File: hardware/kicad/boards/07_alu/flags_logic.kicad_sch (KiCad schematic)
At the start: 14 parts, among them U1 74AHC541, U16 74ACT151, U36 74HC86, U37 74LS08, U38 74LS540, U4 74HC688, U40 74LS377

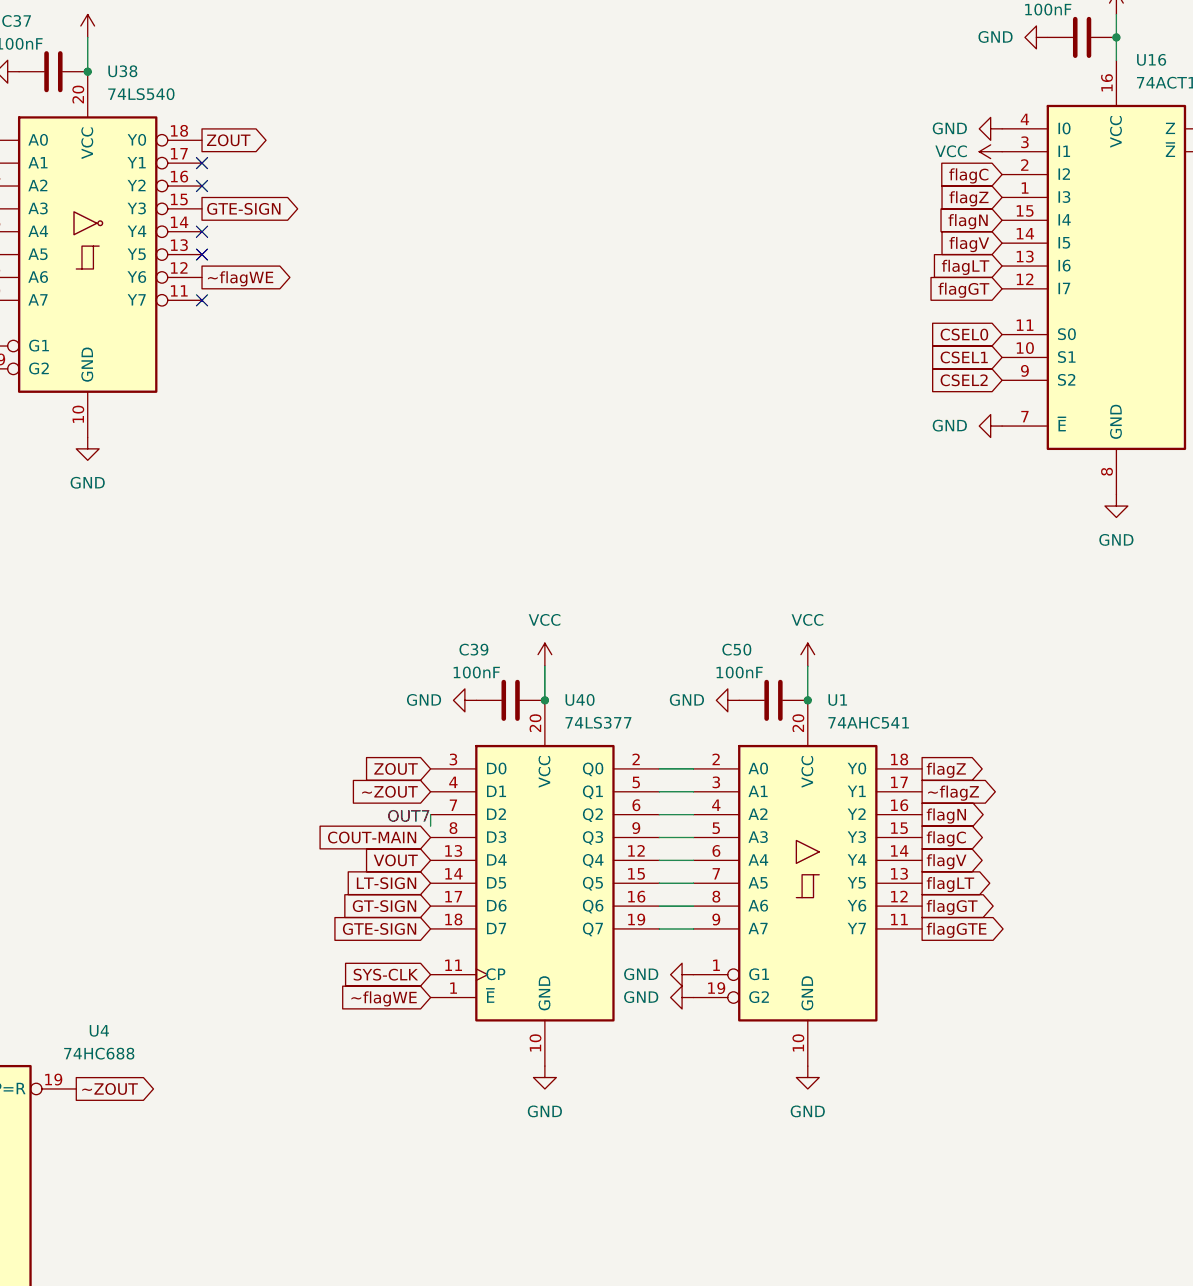
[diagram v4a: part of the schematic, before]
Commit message: checkpoint: routed all but 60 traces
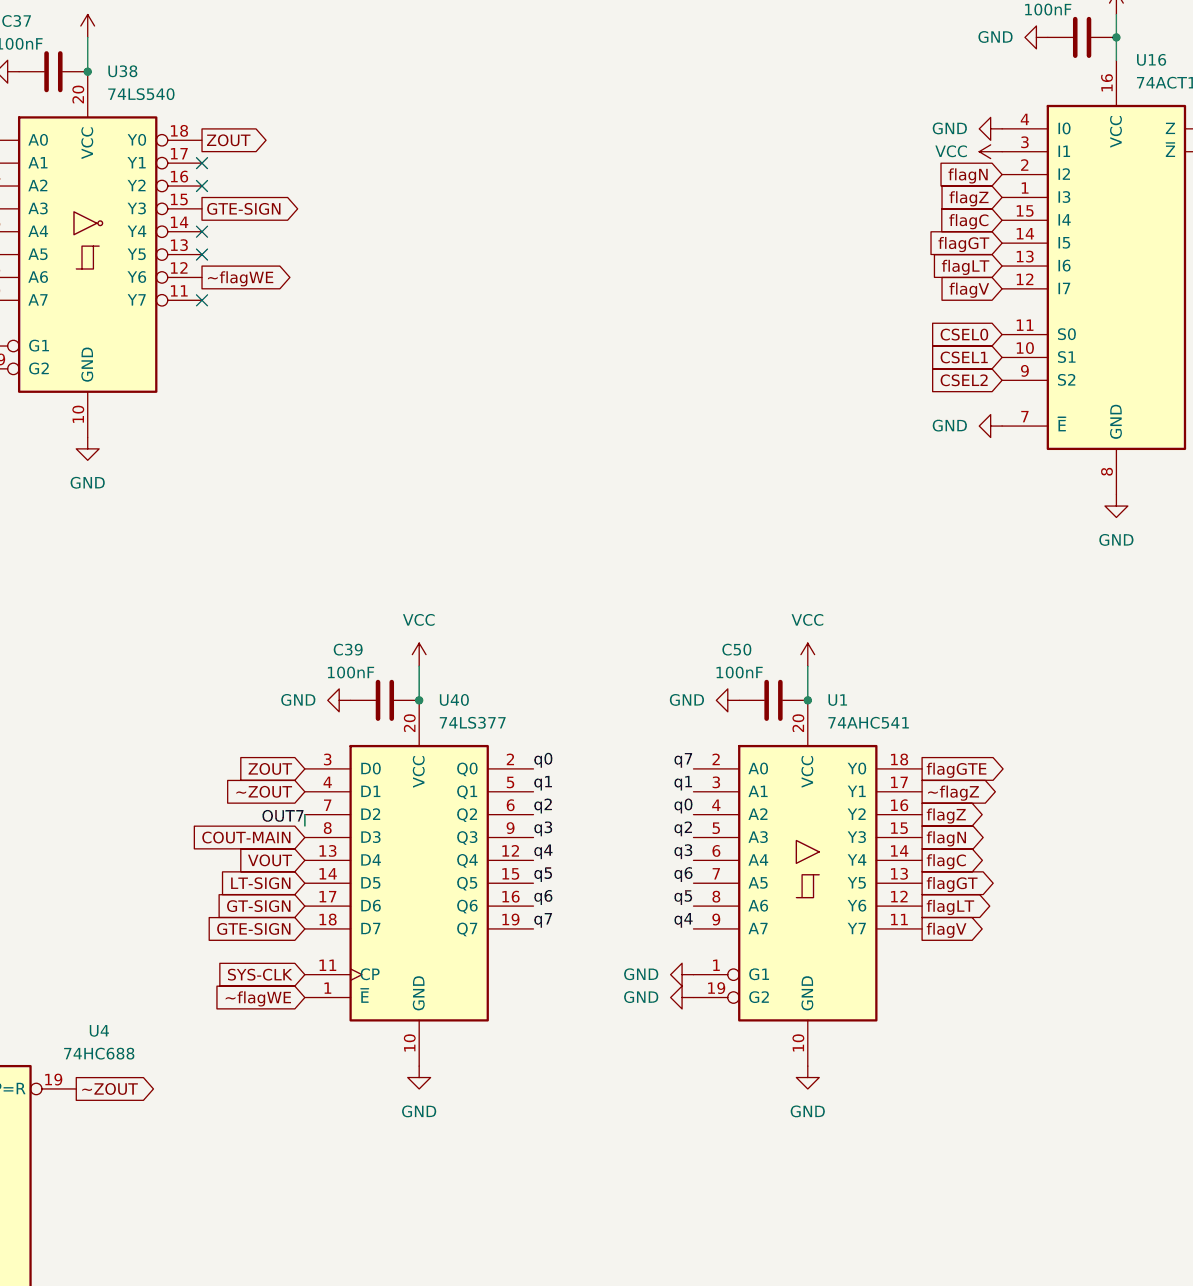
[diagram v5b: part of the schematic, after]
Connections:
- net flagC: now also U1.14 (Y4), U16.15 (I4); no longer U1.15 (Y3), U16.2 (I2)
- net flagGT: now also U1.13 (Y5), U16.14 (I5); no longer U1.12 (Y6), U16.12 (I7)
- net flagGTE: now also U1.18 (Y0); no longer U1.11 (Y7)
- net flagLT: now also U1.12 (Y6); no longer U1.13 (Y5)
- net flagN: now also U1.15 (Y3), U16.2 (I2); no longer U1.16 (Y2), U16.15 (I4)
- net flagV: now also U1.11 (Y7), U16.12 (I7); no longer U1.14 (Y4), U16.14 (I5)
- net flagZ: now also U1.16 (Y2); no longer U1.18 (Y0)
- net q3: now reaches U1.6 (A4)
- net q3: now also U40.9 (Q3); no longer U40.12 (Q4)
- net q5: now reaches U40.15 (Q5)
- net q5: now also U1.8 (A6); no longer U1.7 (A5)
- net q6: now reaches U40.16 (Q6)
- net q6: now also U1.7 (A5); no longer U1.8 (A6)
- net q4: now reaches U1.9 (A7)
- net q4: now also U40.12 (Q4); no longer U40.19 (Q7)
- net q0: now reaches U40.2 (Q0)
- net q0: now also U1.4 (A2); no longer U1.2 (A0)
- net q1: now reaches U1.3 (A1), U40.5 (Q1)
- net q2: now reaches U40.6 (Q2)
- net q2: now also U1.5 (A3); no longer U1.4 (A2)
- new net q7: U1.2 (A0), U40.19 (Q7)
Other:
- moved on the sheet: C39, U40

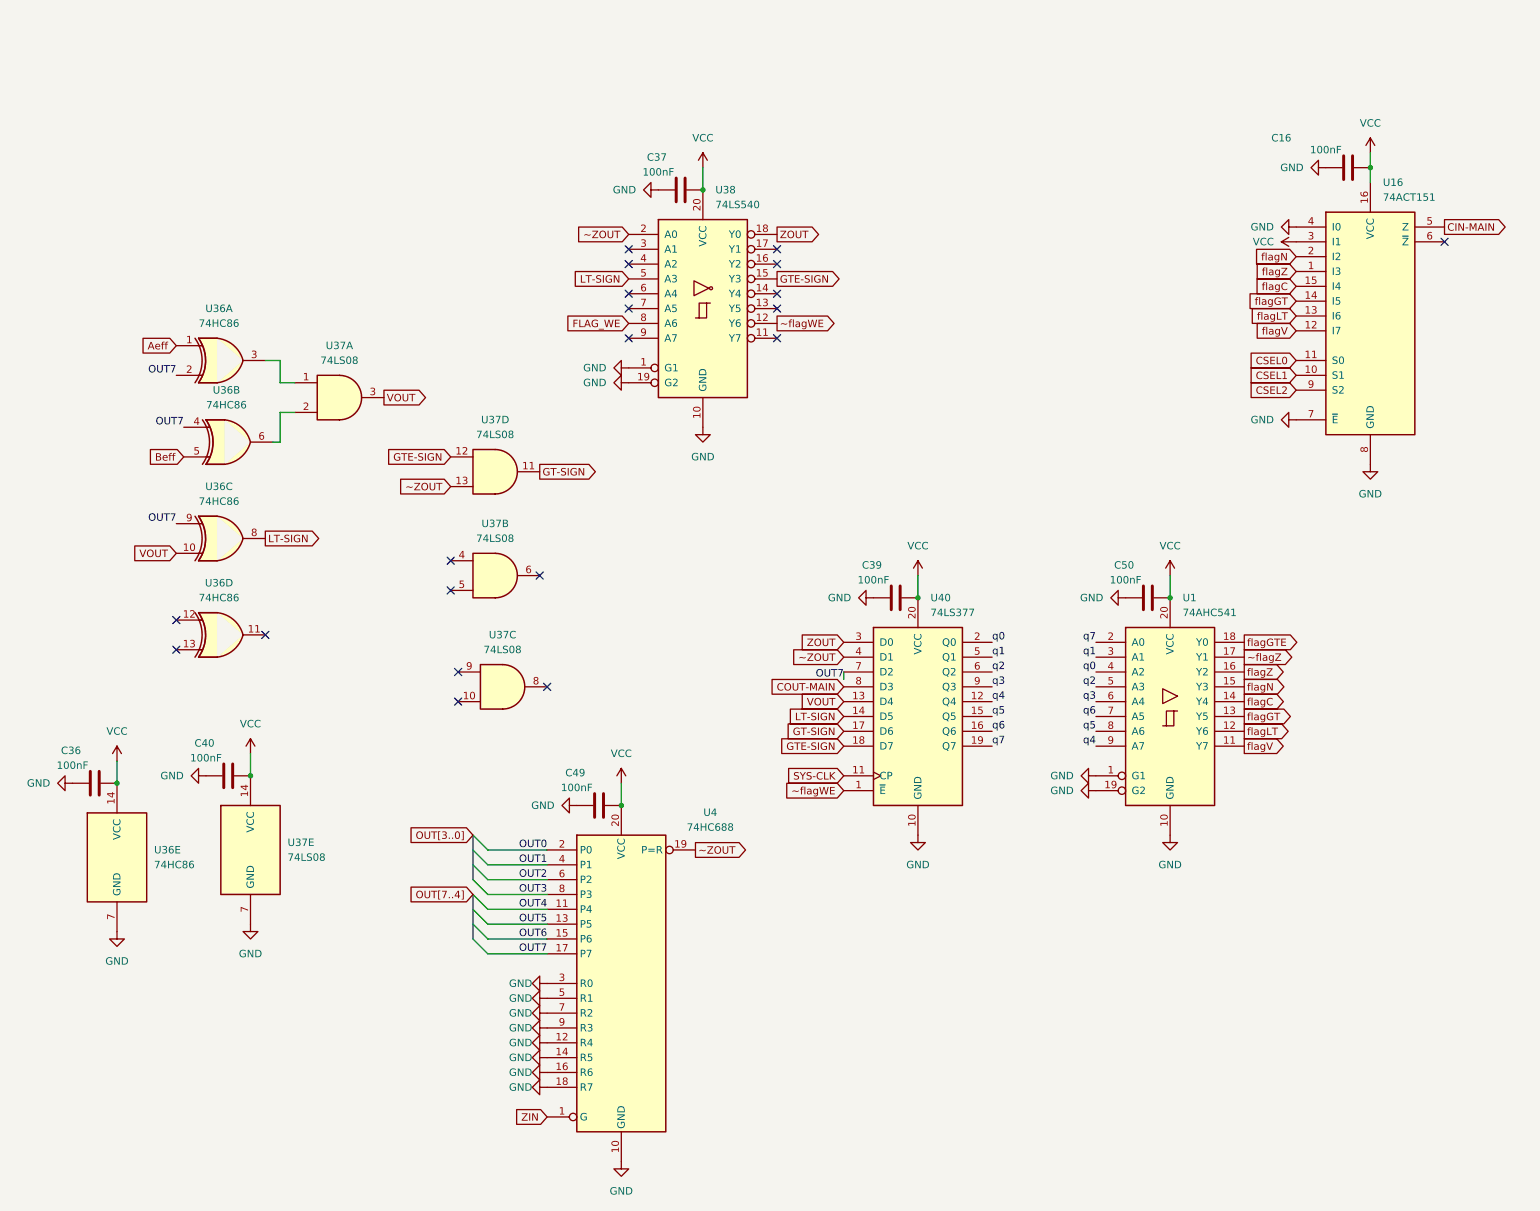
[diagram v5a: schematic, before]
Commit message: fpga: implemented fsm to brute force find matching opcode
It finds opcode by brute force sweeping across 256 by 256 and checking if computed output is equal to expected test output
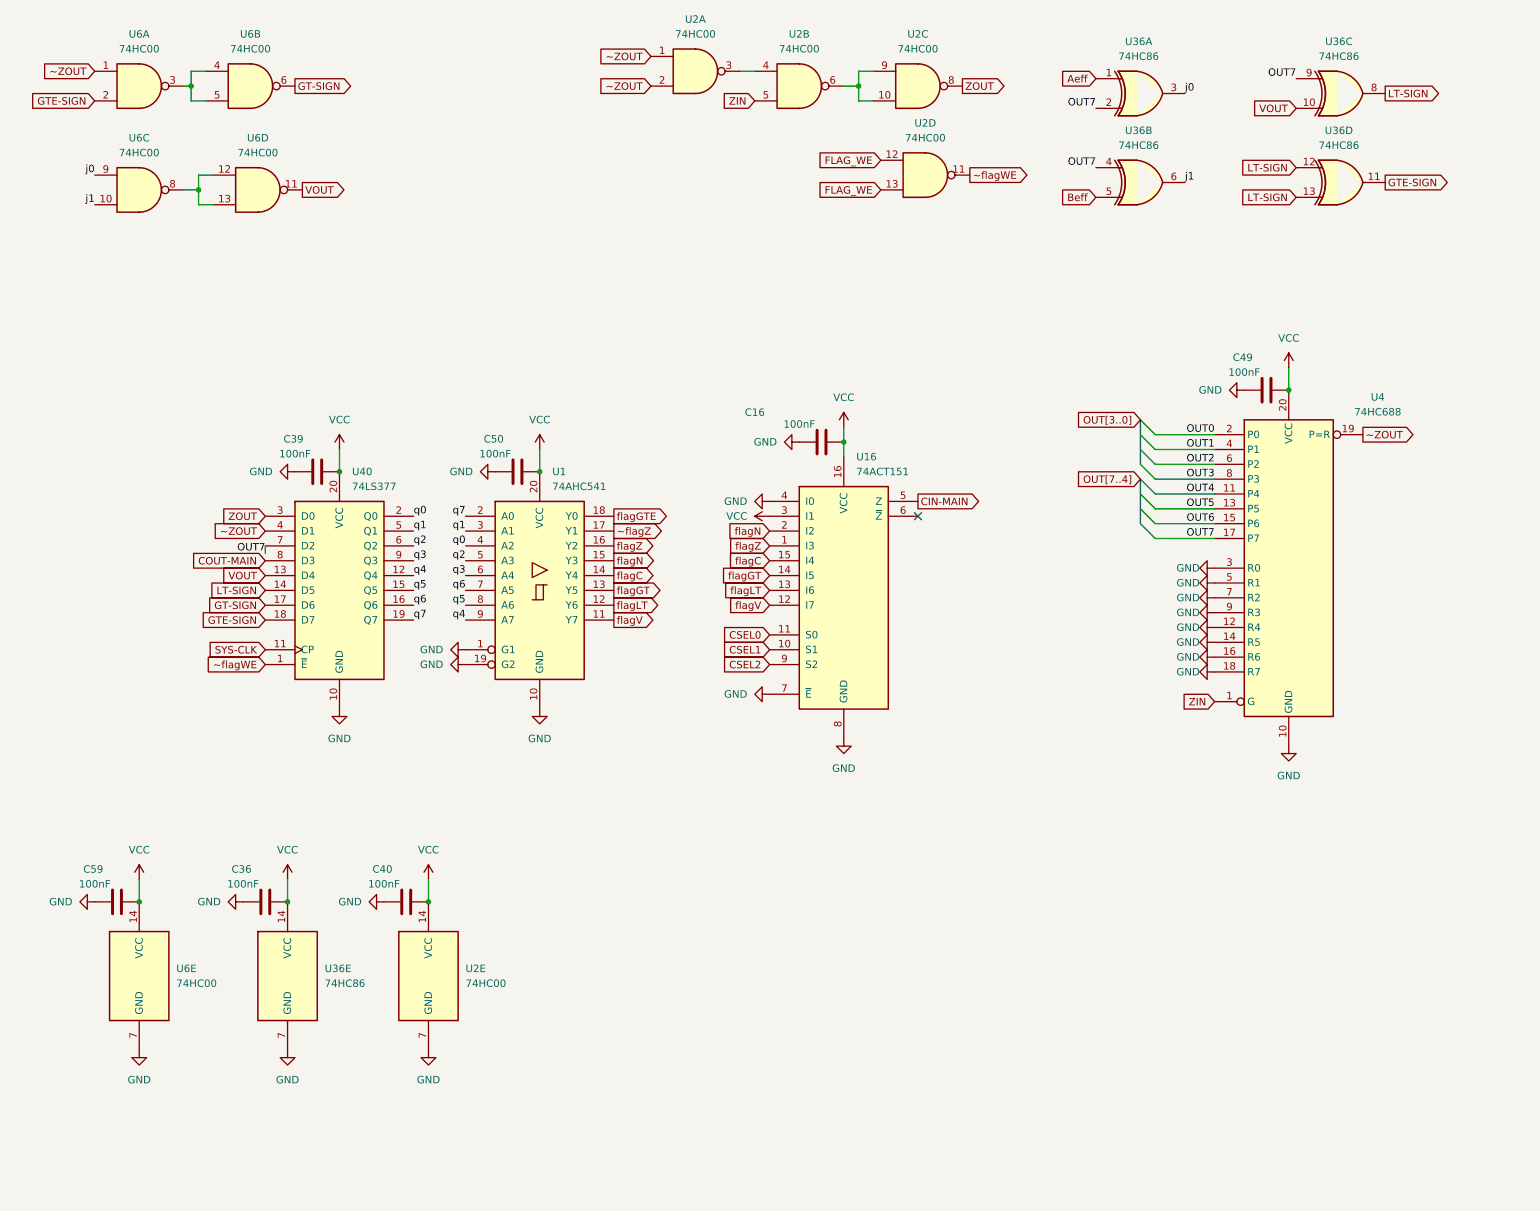
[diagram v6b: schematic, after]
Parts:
- removed C37: 100nF, Capacitor_SMD:C_0603_1608Metric, symbol Device:C
- removed U37: 74LS08, Package_SO:SOIC-14_3.9x8.7mm_P1.27mm, symbol 74xx:74LS08
- removed U38: 74LS540, Package_SO:SOIC-20W_7.5x12.8mm_P1.27mm, symbol 74xx:74LS540
- added C59: 100nF, Capacitor_SMD:C_0603_1608Metric, symbol Device:C
- added U2, U6: 74HC00, Package_SO:SOIC-14_3.9x8.7mm_P1.27mm, symbol 74xx:74HC00
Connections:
- net FLAG_WE: now also U2.12, U2.13
- net GND: now also C59.1, U2.7 (GND), U6.7 (GND)
- net GT-SIGN: now also U6.6
- net GTE-SIGN: now also U36.11, U6.2
- net LT-SIGN: now also U36.12, U36.13
- net VCC: now also C59.2, U2.14 (VCC), U6.14 (VCC)
- net VOUT: now also U6.11
- net ZIN: now also U2.5
- net ZOUT: now also U2.8
- net ~ZOUT: now also U2.1, U2.2, U6.1
- net ~flagWE: now also U2.11
- net j0: now reaches U36.3
- net j0: now also U6.9
- net j1: now reaches U36.6
- net j1: now also U6.10
- new net: U2.3, U2.4
- new net: U2.10, U2.6, U2.9
- new net: U6.12, U6.13, U6.8
- new net: U6.3, U6.4, U6.5
- no-connect marks 20 -> 1
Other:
- moved on the sheet: C16, C36, C39, C40, C49, C50, U1, U16, U36A, U36B, U36C, U36D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

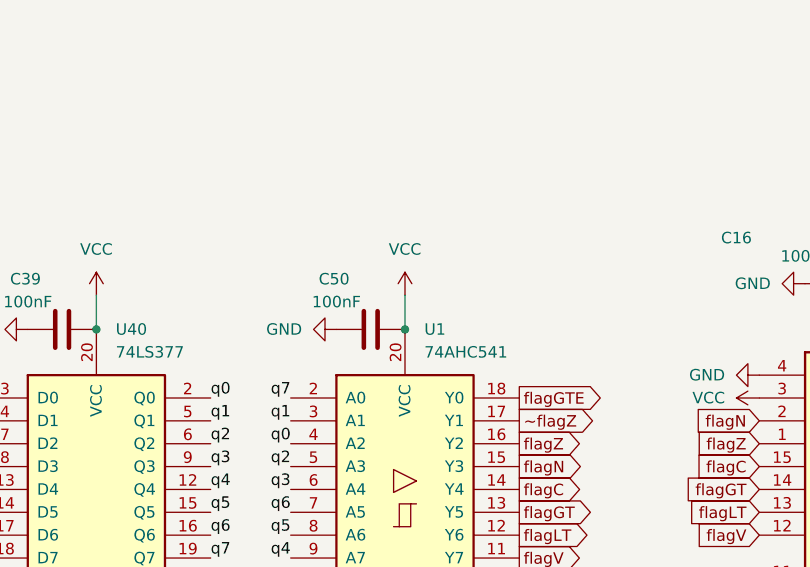
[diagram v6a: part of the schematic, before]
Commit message: fix: updated the flag logic to match simulation in digital design
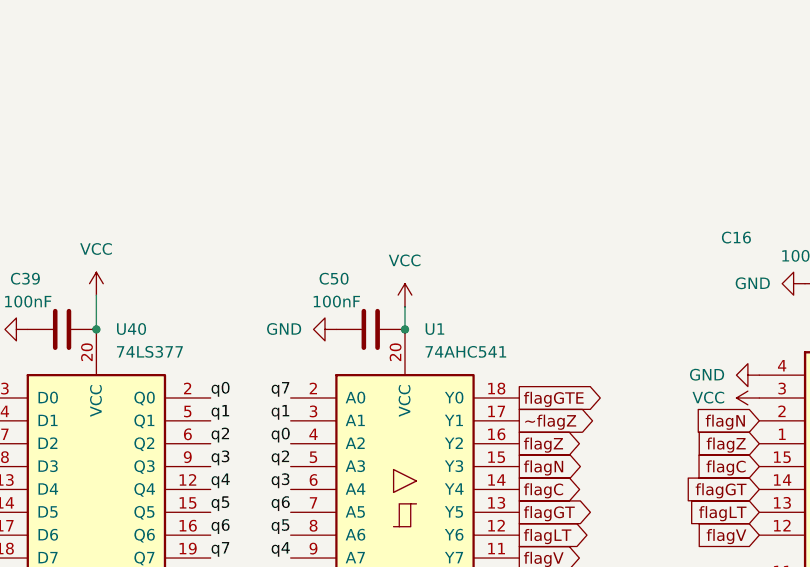
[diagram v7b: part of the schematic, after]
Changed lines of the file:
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@@
 	(paper "A4")
 	(junction
-		(at 104.14 90.17)
-		(diameter 0)
-		(color 0 0 0 0)
-	)
-	(junction
 		(at 35.56 163.83)
 		(diameter 0)
@@
 		(color 0 0 0 0)
 	)
+	(junction
+		(at 104.14 90.17)
+		(diameter 0)
+		(color 0 0 0 0)
+	)
 	(no_connect
 		(at 168.91 97.79)
@@
 	(wire
 		(pts
-			(xy 104.14 86.36) (xy 104.14 90.17)
+			(xy 104.14 87.63) (xy 104.14 90.17)
 		)
 		(stroke
@@
 	(symbol
 		(lib_id "power:VCC")
-		(at 104.14 86.36 0)
+		(at 104.14 87.63 0)
 		(unit 1)
 		(body_style 1)
@@
 		(fields_autoplaced yes)
 		(property "Reference" "#PWR086"
-			(at 104.14 90.17 0)
+			(at 104.14 91.44 0)
 			(hide yes)
 			(show_name no)
@@
 		)
 		(property "Value" "VCC"
-			(at 104.14 81.28 0)
+			(at 104.14 82.55 0)
 			(show_name no)
 			(do_not_autoplace no)
@@
 		)
 		(property "Footprint" ""
-			(at 104.14 86.36 0)
+			(at 104.14 87.63 0)
 			(hide yes)
 			(show_name no)
@@
 		)
 		(property "Datasheet" ""
-			(at 104.14 86.36 0)
+			(at 104.14 87.63 0)
 			(hide yes)
 			(show_name no)
@@
 		)
 		(property "Description" "Power symbol creates a global label with name \"VCC\""
-			(at 104.14 86.36 0)
+			(at 104.14 87.63 0)
 			(hide yes)
 			(show_name no)
